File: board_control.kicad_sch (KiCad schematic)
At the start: 14 parts, among them SW1 PRGM, U4 ESP-12F

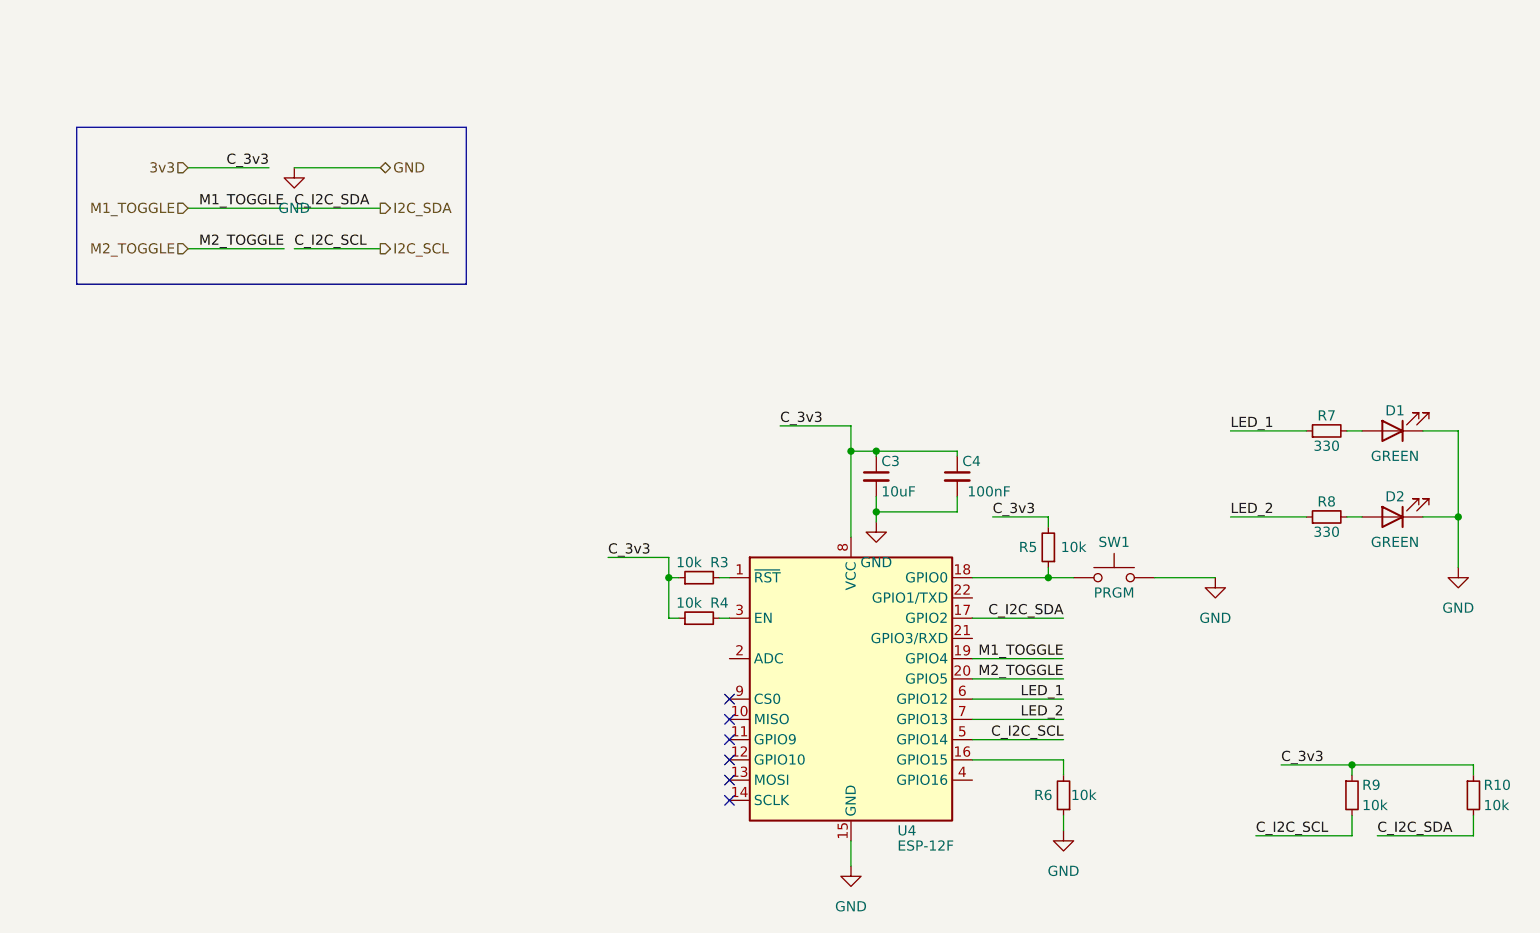
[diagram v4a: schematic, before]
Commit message: Added TX/RX to schematic. Updated PCB
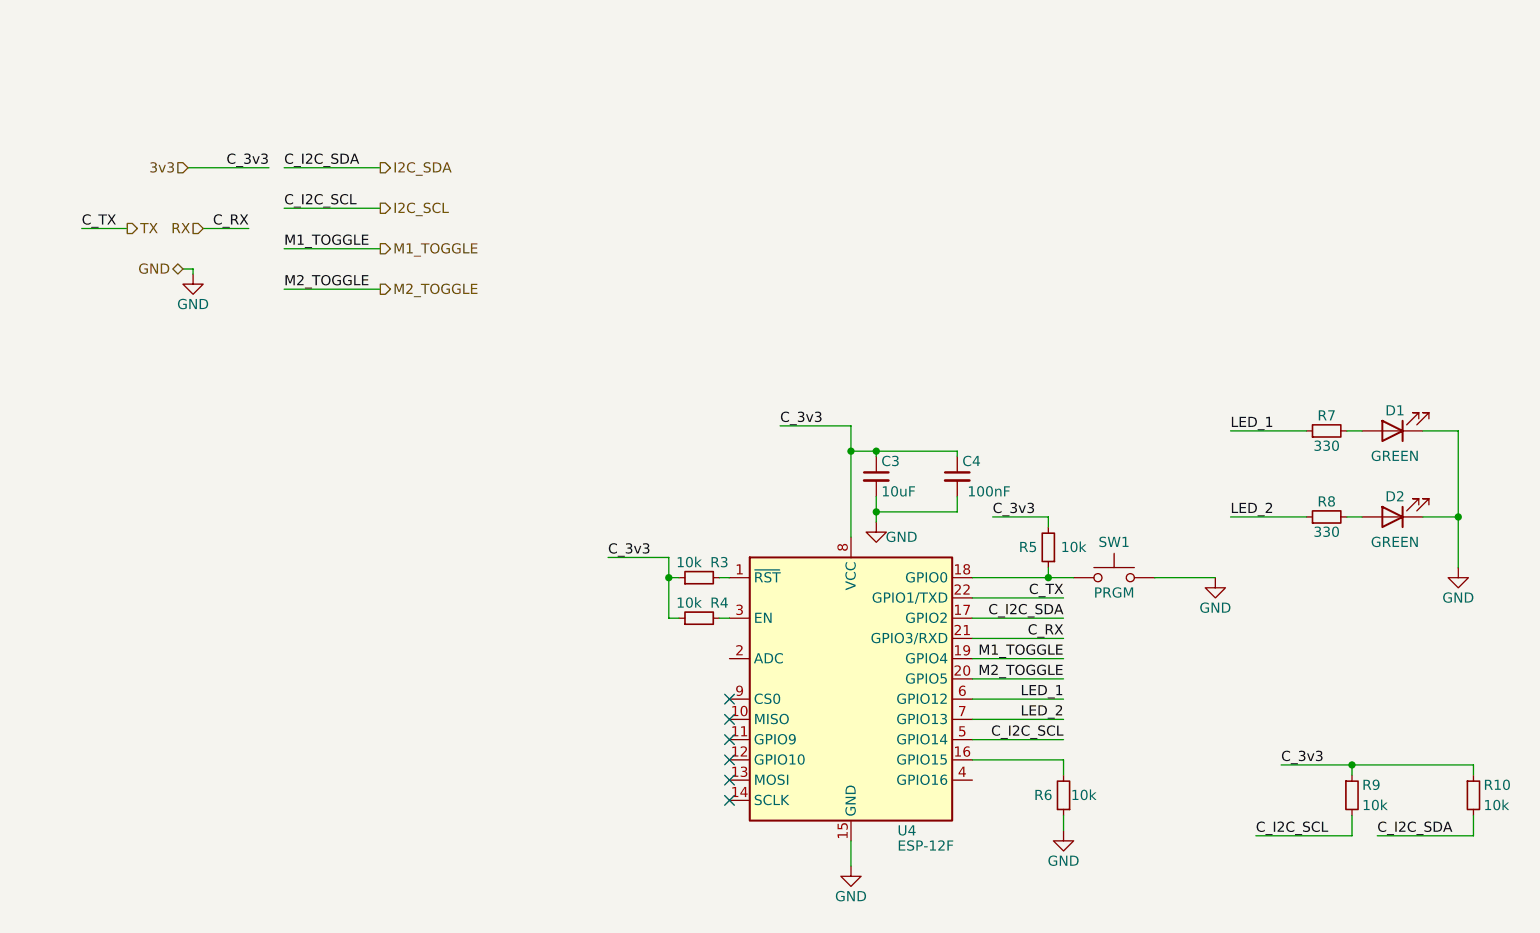
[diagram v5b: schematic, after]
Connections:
- net RX: now reaches U4.21 (GPIO3/RXD)
- net TX: now reaches U4.22 (GPIO1/TXD)

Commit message: Added more GND vias, fixed incorrect net trace sizing
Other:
- title: (none) -> Smart USB Port
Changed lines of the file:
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@@
 (kicad_sch (version 20211123) (generator eeschema)
   (paper "A4")
+  (title_block
+    (title "Smart USB Port")
+    (date "2022-10-23")
+    (rev "0.1")
+  )
   (junction (at 118.11 66.675) (diameter 0) (color 0 0 0 0)
   )

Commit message: Updated some components to use ones I already own
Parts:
- C3: LCSC Part Number C100042 -> C19702; Manufacturer YAGEO -> Samsung Electro-Mechanics; Manufacturer Part Number CC0603KRX7R9BB103 -> CL10A106KP8NNNC
- C4: LCSC Part Number C30926 -> C1591; Manufacturer FH (Guangdong Fenghua Advanced Tech) -> Samsung Electro-Mechanics; Manufacturer Part Number 0603B104K500NT -> CL10B104KB8NNNC
- D1, D2: footprint LED_SMD:LED_0805_2012Metric -> LED_SMD:LED_0603_1608Metric; LCSC Part Number C434432 -> C72043; Manufacturer Yongyu Photoelectric -> Everlight Elec; Manufacturer Part Number SZYY0805G -> 19-217/GHC-YR1S2/3T
- R7, R8: LCSC Part Number C25229 -> C105881; Manufacturer UNI-ROYAL(Uniroyal Elec) -> YAGEO; Manufacturer Part Number 0603WAJ0301T5E -> RC0603FR-07330RL
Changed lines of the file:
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@@
       (effects (font (size 1.27 1.27)) hide)
     )
-    (property "LCSC Part Number" "C30926" (id 4) (at 131.445 69.85 0)
+    (property "LCSC Part Number" "C1591" (id 4) (at 131.445 69.85 0)
       (effects (font (size 1.27 1.27)) hide)
     )
-    (property "Manufacturer" "FH (Guangdong Fenghua Advanced Tech)" (id 5) (at 131.445 69.85 0)
+    (property "Manufacturer" "Samsung Electro-Mechanics" (id 5) (at 131.445 69.85 0)
       (effects (font (size 1.27 1.27)) hide)
     )
-    (property "Manufacturer Part Number" "0603B104K500NT" (id 6) (at 131.445 69.85 0)
+    (property "Manufacturer Part Number" "CL10B104KB8NNNC" (id 6) (at 131.445 69.85 0)
       (effects (font (size 1.27 1.27)) hide)
     )
@@
       (effects (font (size 1.27 1.27)) hide)
     )
-    (property "LCSC Part Number" "C25229" (id 4) (at 177.8 74.93 0)
+    (property "LCSC Part Number" "C105881" (id 4) (at 177.8 74.93 0)
       (effects (font (size 1.27 1.27)) hide)
     )
-    (property "Manufacturer" "UNI-ROYAL(Uniroyal Elec)" (id 5) (at 177.8 74.93 0)
+    (property "Manufacturer" "YAGEO" (id 5) (at 177.8 74.93 0)
       (effects (font (size 1.27 1.27)) hide)
     )
-    (property "Manufacturer Part Number" "0603WAJ0301T5E" (id 6) (at 177.8 74.93 0)
+    (property "Manufacturer Part Number" "RC0603FR-07330RL" (id 6) (at 177.8 74.93 0)
       (effects (font (size 1.27 1.27)) hide)
     )
@@
       (effects (font (size 1.27 1.27)) hide)
     )
-    (property "LCSC Part Number" "C100042" (id 4) (at 121.285 69.85 0)
+    (property "LCSC Part Number" "C19702" (id 4) (at 121.285 69.85 0)
       (effects (font (size 1.27 1.27)) hide)
     )
-    (property "Manufacturer" "YAGEO" (id 5) (at 121.285 69.85 0)
+    (property "Manufacturer" "Samsung Electro-Mechanics" (id 5) (at 121.285 69.85 0)
       (effects (font (size 1.27 1.27)) hide)
     )
-    (property "Manufacturer Part Number" "CC0603KRX7R9BB103" (id 6) (at 121.285 69.85 0)
+    (property "Manufacturer Part Number" "CL10A106KP8NNNC" (id 6) (at 121.285 69.85 0)
       (effects (font (size 1.27 1.27)) hide)
     )
@@
       (effects (font (size 1.27 1.27)) hide)
     )
-    (property "LCSC Part Number" "C25229" (id 4) (at 177.8 64.135 0)
+    (property "LCSC Part Number" "C105881" (id 4) (at 177.8 64.135 0)
       (effects (font (size 1.27 1.27)) hide)
     )
-    (property "Manufacturer" "UNI-ROYAL(Uniroyal Elec)" (id 5) (at 177.8 64.135 0)
+    (property "Manufacturer" "YAGEO" (id 5) (at 177.8 64.135 0)
       (effects (font (size 1.27 1.27)) hide)
     )
-    (property "Manufacturer Part Number" "0603WAJ0301T5E" (id 6) (at 177.8 64.135 0)
+    (property "Manufacturer Part Number" "RC0603FR-07330RL" (id 6) (at 177.8 64.135 0)
       (effects (font (size 1.27 1.27)) hide)
     )
@@
     (property "Reference" "D1" (id 0) (at 186.3725 61.595 0))
     (property "Value" "GREEN" (id 1) (at 186.3725 67.31 0))
-    (property "Footprint" "LED_SMD:LED_0805_2012Metric" (id 2) (at 186.055 64.135 0)
+    (property "Footprint" "LED_SMD:LED_0603_1608Metric" (id 2) (at 186.055 64.135 0)
       (effects (font (size 1.27 1.27)) hide)
     )
@@
       (effects (font (size 1.27 1.27)) hide)
     )
-    (property "LCSC Part Number" "C434432" (id 4) (at 186.055 64.135 0)
+    (property "LCSC Part Number" "C72043" (id 4) (at 186.055 64.135 0)
       (effects (font (size 1.27 1.27)) hide)
     )
-    (property "Manufacturer" "Yongyu Photoelectric" (id 5) (at 186.055 64.135 0)
+    (property "Manufacturer" "Everlight Elec" (id 5) (at 186.055 64.135 0)
       (effects (font (size 1.27 1.27)) hide)
     )
-    (property "Manufacturer Part Number" "SZYY0805G" (id 6) (at 186.055 64.135 0)
+    (property "Manufacturer Part Number" "19-217/GHC-YR1S2/3T" (id 6) (at 186.055 64.135 0)
       (effects (font (size 1.27 1.27)) hide)
     )
@@
     (property "Reference" "D2" (id 0) (at 186.3725 72.39 0))
     (property "Value" "GREEN" (id 1) (at 186.3725 78.105 0))
-    (property "Footprint" "LED_SMD:LED_0805_2012Metric" (id 2) (at 186.055 74.93 0)
+    (property "Footprint" "LED_SMD:LED_0603_1608Metric" (id 2) (at 186.055 74.93 0)
       (effects (font (size 1.27 1.27)) hide)
     )
@@
       (effects (font (size 1.27 1.27)) hide)
     )
-    (property "LCSC Part Number" "C434432" (id 4) (at 186.055 74.93 0)
+    (property "LCSC Part Number" "C72043" (id 4) (at 186.055 74.93 0)
       (effects (font (size 1.27 1.27)) hide)
     )
-    (property "Manufacturer" "Yongyu Photoelectric" (id 5) (at 186.055 74.93 0)
+    (property "Manufacturer" "Everlight Elec" (id 5) (at 186.055 74.93 0)
       (effects (font (size 1.27 1.27)) hide)
     )
-    (property "Manufacturer Part Number" "SZYY0805G" (id 6) (at 186.055 74.93 0)
+    (property "Manufacturer Part Number" "19-217/GHC-YR1S2/3T" (id 6) (at 186.055 74.93 0)
       (effects (font (size 1.27 1.27)) hide)
     )

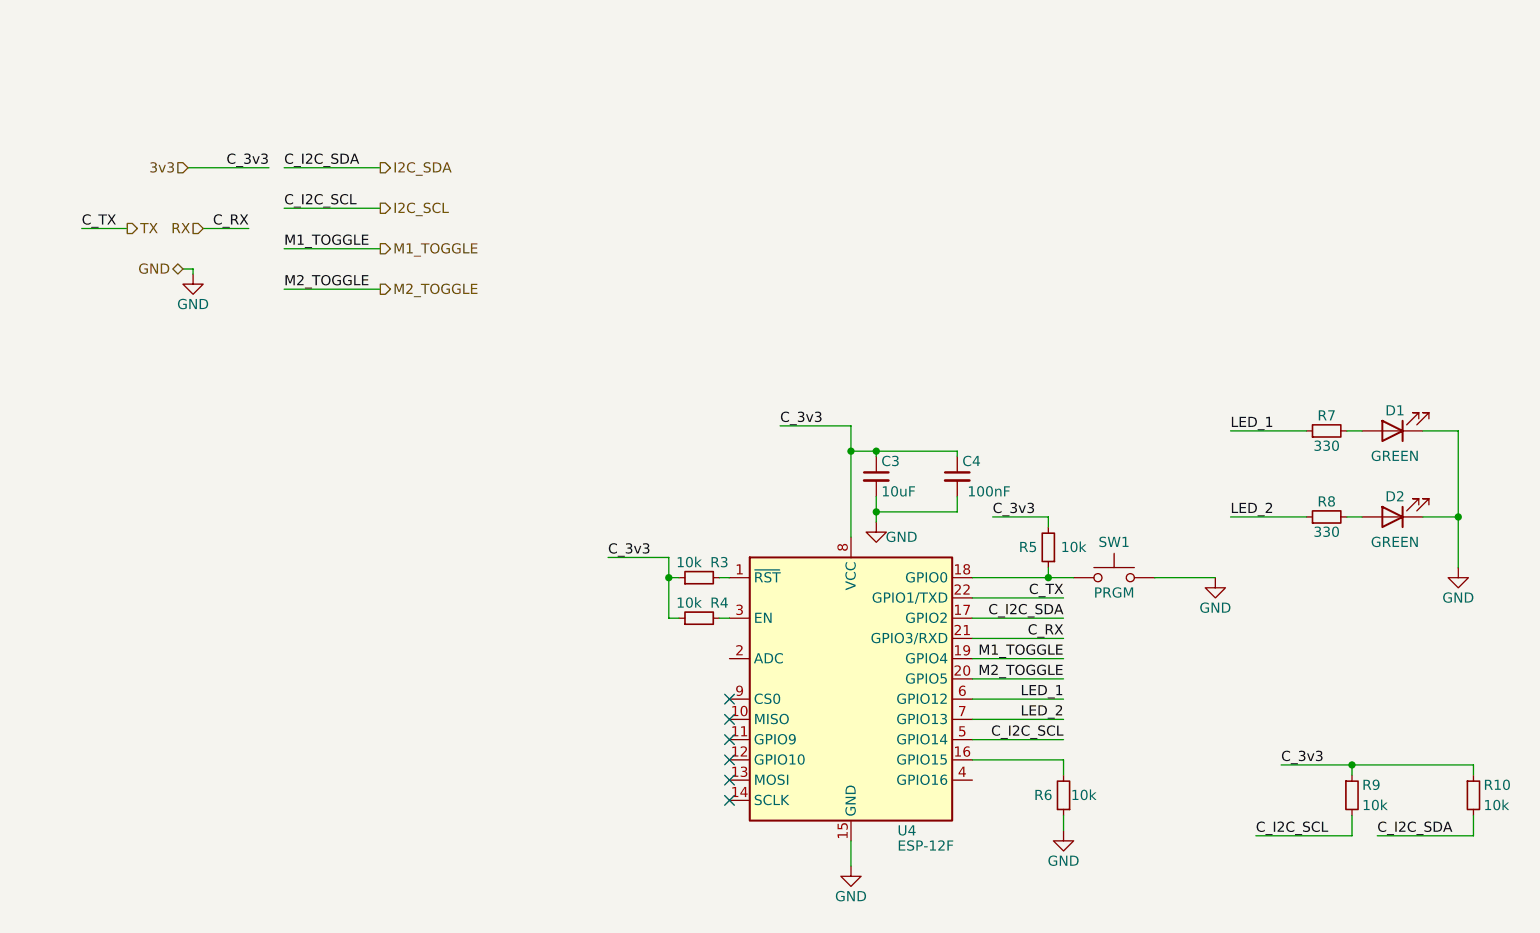
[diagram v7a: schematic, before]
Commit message: Made schematics pretty, added photos, added README
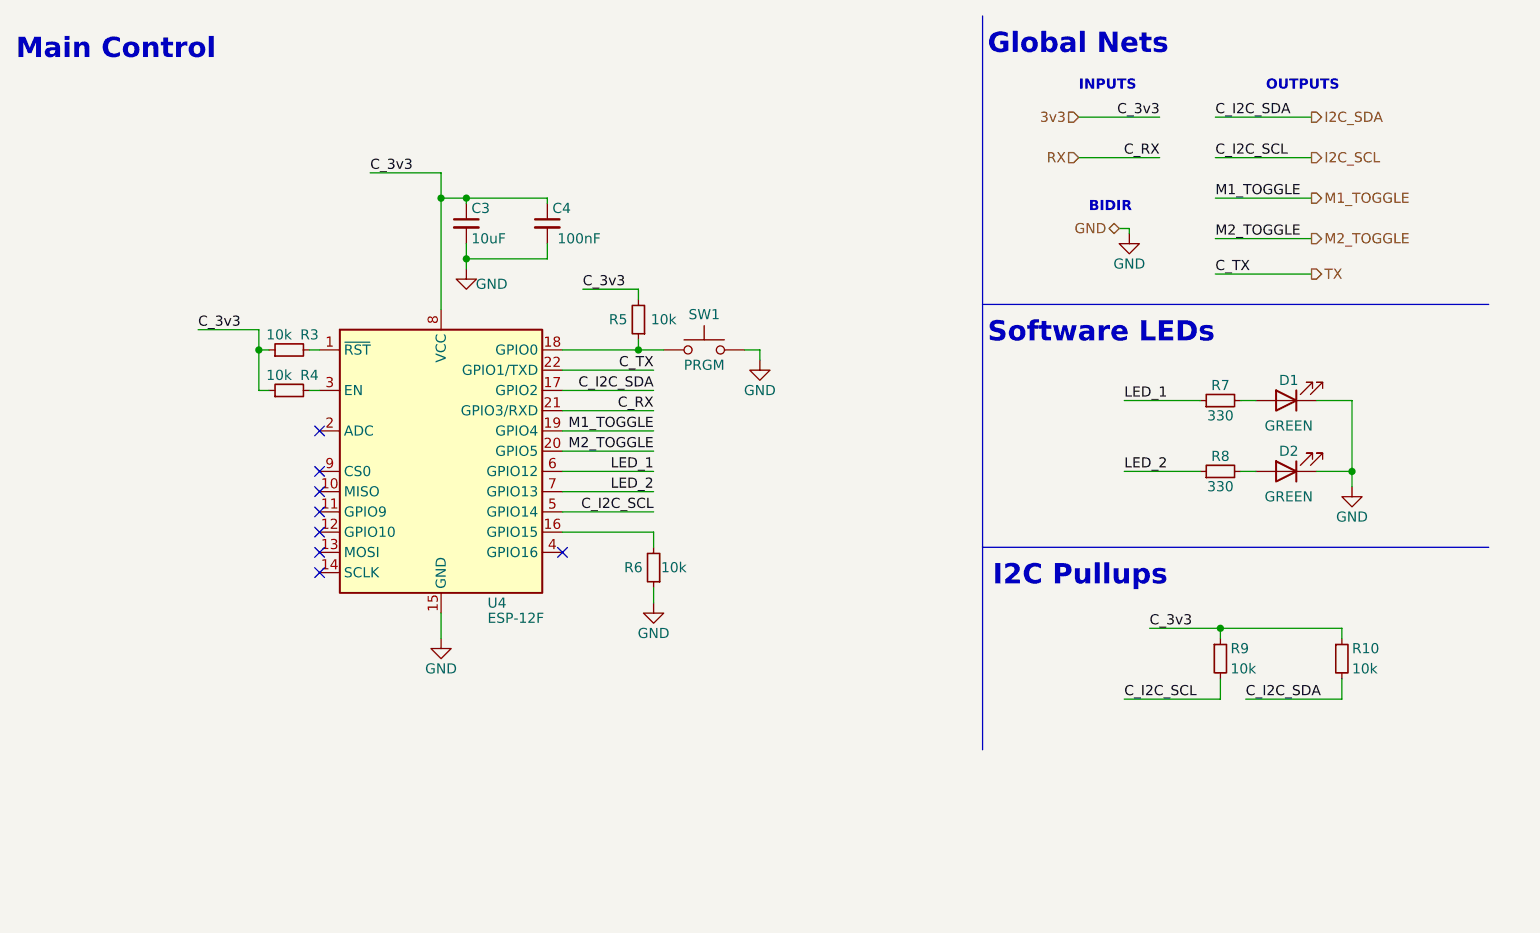
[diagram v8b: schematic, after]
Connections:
- no-connect marks 6 -> 8
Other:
- note added: "BIDIR"
- note added: "Global Nets"
- note added: "I2C Pullups"
- note added: "INPUTS"
- note added: "Main Control"
- note added: "OUTPUTS"
- note added: "Software LEDs"
- title: Smart USB Port -> Wifi USB Port
- moved on the sheet: C3, C4, D1, D2, R10, R3, R4, R5, R6, R7, R8, R9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
